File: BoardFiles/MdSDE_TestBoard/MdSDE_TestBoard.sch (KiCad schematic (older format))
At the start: 14 parts

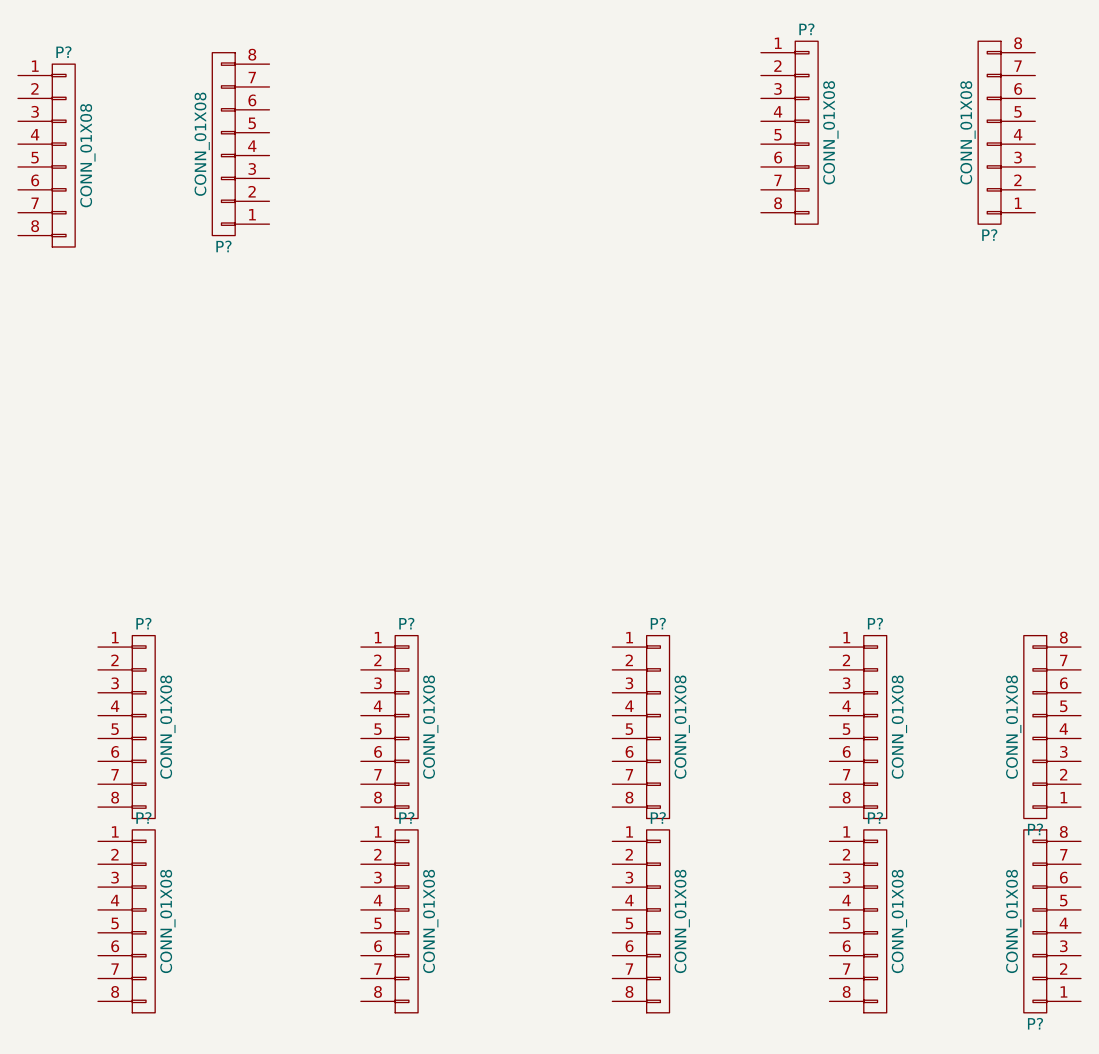
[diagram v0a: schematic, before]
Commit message: Built motor driver carrier
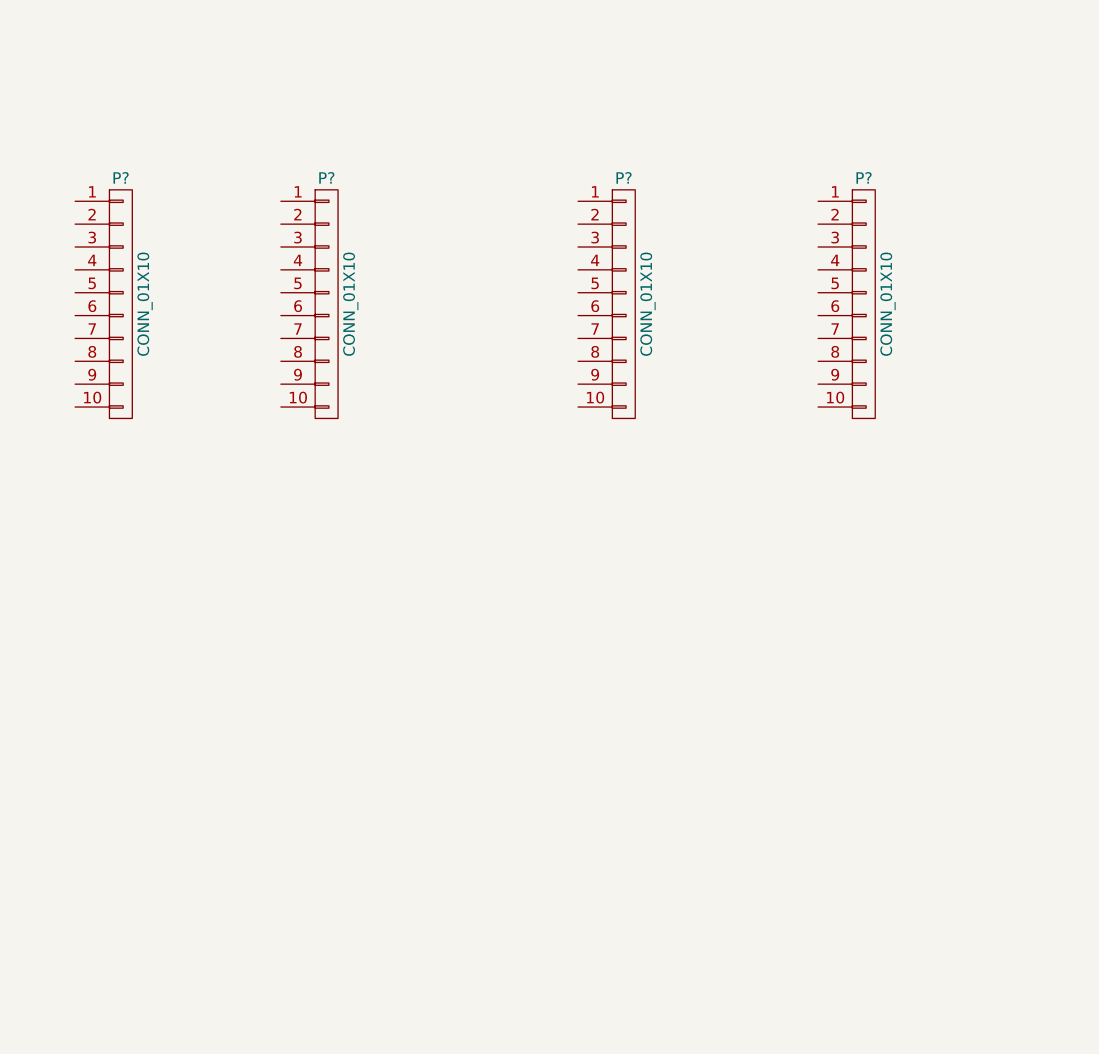
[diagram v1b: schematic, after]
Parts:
- removed P? (x14): CONN_01X08, symbol CONN_01X08
- added P? (x4): CONN_01X10, symbol CONN_01X10
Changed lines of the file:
@@
 LIBS:contrib
 LIBS:valves
+LIBS:MdSDE_TestBoard-cache
 EELAYER 25 0
 EELAYER END
@@
 $EndDescr
 $Comp
-L CONN_01X08 P?
-U 1 1 56D884A4
-P 2200 1700
-F 0 "P?" H 2200 2150 50  0000 C CNN
-F 1 "CONN_01X08" V 2300 1700 50  0000 C CNN
-F 2 "" H 2200 1700 60  0000 C CNN
-F 3 "" H 2200 1700 60  0000 C CNN
-	1    2200 1700
+L CONN_01X10 P?
+U 1 1 56EC1E59
+P 2450 2350
+F 0 "P?" H 2450 2900 50  0000 C CNN
+F 1 "CONN_01X10" V 2550 2350 50  0000 C CNN
+F 2 "" H 2450 2350 50  0000 C CNN
+F 3 "" H 2450 2350 50  0000 C CNN
+	1    2450 2350
 	1    0    0    -1
 $EndComp
 $Comp
-L CONN_01X08 P?
-U 1 1 56D884DC
-P 2900 1650
-F 0 "P?" H 2900 2100 50  0000 C CNN
-F 1 "CONN_01X08" V 3000 1650 50  0000 C CNN
-F 2 "" H 2900 1650 60  0000 C CNN
-F 3 "" H 2900 1650 60  0000 C CNN
-	1    2900 1650
-	-1   0    0    1
-$EndComp
-$Comp
-L CONN_01X08 P?
-U 1 1 56D88507
-P 5450 1600
-F 0 "P?" H 5450 2050 50  0000 C CNN
-F 1 "CONN_01X08" V 5550 1600 50  0000 C CNN
-F 2 "" H 5450 1600 60  0000 C CNN
-F 3 "" H 5450 1600 60  0000 C CNN
-	1    5450 1600
+L CONN_01X10 P?
+U 1 1 56EC1ED5
+P 3350 2350
+F 0 "P?" H 3350 2900 50  0000 C CNN
+F 1 "CONN_01X10" V 3450 2350 50  0000 C CNN
+F 2 "" H 3350 2350 50  0000 C CNN
+F 3 "" H 3350 2350 50  0000 C CNN
+	1    3350 2350
 	1    0    0    -1
 $EndComp
 $Comp
-L CONN_01X08 P?
-U 1 1 56D8853D
-P 6250 1600
-F 0 "P?" H 6250 2050 50  0000 C CNN
-F 1 "CONN_01X08" V 6350 1600 50  0000 C CNN
-F 2 "" H 6250 1600 60  0000 C CNN
-F 3 "" H 6250 1600 60  0000 C CNN
-	1    6250 1600
-	-1   0    0    1
-$EndComp
-$Comp
-L CONN_01X08 P?
-U 1 1 56D88577
-P 5750 4200
-F 0 "P?" H 5750 4650 50  0000 C CNN
-F 1 "CONN_01X08" V 5850 4200 50  0000 C CNN
-F 2 "" H 5750 4200 60  0000 C CNN
-F 3 "" H 5750 4200 60  0000 C CNN
-	1    5750 4200
+L CONN_01X10 P?
+U 1 1 56EC1F49
+P 4650 2350
+F 0 "P?" H 4650 2900 50  0000 C CNN
+F 1 "CONN_01X10" V 4750 2350 50  0000 C CNN
+F 2 "" H 4650 2350 50  0000 C CNN
+F 3 "" H 4650 2350 50  0000 C CNN
+	1    4650 2350
 	1    0    0    -1
 $EndComp
 $Comp
-L CONN_01X08 P?
-U 1 1 56D885C6
-P 5750 5050
-F 0 "P?" H 5750 5500 50  0000 C CNN
-F 1 "CONN_01X08" V 5850 5050 50  0000 C CNN
-F 2 "" H 5750 5050 60  0000 C CNN
-F 3 "" H 5750 5050 60  0000 C CNN
-	1    5750 5050
+L CONN_01X10 P?
+U 1 1 56EC1F98
+P 5700 2350
+F 0 "P?" H 5700 2900 50  0000 C CNN
+F 1 "CONN_01X10" V 5800 2350 50  0000 C CNN
+F 2 "" H 5700 2350 50  0000 C CNN
+F 3 "" H 5700 2350 50  0000 C CNN
+	1    5700 2350
 	1    0    0    -1
 $EndComp
-$Comp
-L CONN_01X08 P?
-U 1 1 56D8860F
-P 6450 4200
-F 0 "P?" H 6450 4650 50  0000 C CNN
-F 1 "CONN_01X08" V 6550 4200 50  0000 C CNN
-F 2 "" H 6450 4200 60  0000 C CNN
-F 3 "" H 6450 4200 60  0000 C CNN
-	1    6450 4200
-	-1   0    0    1
-$EndComp
-$Comp
-L CONN_01X08 P?
-U 1 1 56D88657
-P 6450 5050
-F 0 "P?" H 6450 5500 50  0000 C CNN
-F 1 "CONN_01X08" V 6550 5050 50  0000 C CNN
-F 2 "" H 6450 5050 60  0000 C CNN
-F 3 "" H 6450 5050 60  0000 C CNN
-	1    6450 5050
-	-1   0    0    1
-$EndComp
-$Comp
-L CONN_01X08 P?
-U 1 1 56D8868F
-P 4800 4200
-F 0 "P?" H 4800 4650 50  0000 C CNN
-F 1 "CONN_01X08" V 4900 4200 50  0000 C CNN
-F 2 "" H 4800 4200 60  0000 C CNN
-F 3 "" H 4800 4200 60  0000 C CNN
-	1    4800 4200
-	1    0    0    -1
-$EndComp
-$Comp
-L CONN_01X08 P?
-U 1 1 56D886CB
-P 4800 5050
-F 0 "P?" H 4800 5500 50  0000 C CNN
-F 1 "CONN_01X08" V 4900 5050 50  0000 C CNN
-F 2 "" H 4800 5050 60  0000 C CNN
-F 3 "" H 4800 5050 60  0000 C CNN
-	1    4800 5050
-	1    0    0    -1
-$EndComp
-$Comp
-L CONN_01X08 P?
-U 1 1 56D889F3
-P 3700 4200
-F 0 "P?" H 3700 4650 50  0000 C CNN
-F 1 "CONN_01X08" V 3800 4200 50  0000 C CNN
-F 2 "" H 3700 4200 60  0000 C CNN
-F 3 "" H 3700 4200 60  0000 C CNN
-	1    3700 4200
-	1    0    0    -1
-$EndComp
-$Comp
-L CONN_01X08 P?
-U 1 1 56D88A33
-P 2550 4200
-F 0 "P?" H 2550 4650 50  0000 C CNN
-F 1 "CONN_01X08" V 2650 4200 50  0000 C CNN
-F 2 "" H 2550 4200 60  0000 C CNN
-F 3 "" H 2550 4200 60  0000 C CNN
-	1    2550 4200
-	1    0    0    -1
-$EndComp
-$Comp
-L CONN_01X08 P?
-U 1 1 56D88A78
-P 3700 5050
-F 0 "P?" H 3700 5500 50  0000 C CNN
-F 1 "CONN_01X08" V 3800 5050 50  0000 C CNN
-F 2 "" H 3700 5050 60  0000 C CNN
-F 3 "" H 3700 5050 60  0000 C CNN
-	1    3700 5050
-	1    0    0    -1
-$EndComp
-$Comp
-L CONN_01X08 P?
-U 1 1 56D88AC1
-P 2550 5050
-F 0 "P?" H 2550 5500 50  0000 C CNN
-F 1 "CONN_01X08" V 2650 5050 50  0000 C CNN
-F 2 "" H 2550 5050 60  0000 C CNN
-F 3 "" H 2550 5050 60  0000 C CNN
-	1    2550 5050
-	1    0    0    -1
-$EndComp
